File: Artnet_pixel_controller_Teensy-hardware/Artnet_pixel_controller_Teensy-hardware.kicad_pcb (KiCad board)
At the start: 2 copper layers, 122 x 57 mm, 37 parts, among them J1 Barrel_Jack_Switch, J10 Conn_01x02_Pin, J2 HR871181A, J3 Conn_01x02_Pin, J4 Conn_01x02_Pin, J5 Conn_01x02_Pin, J6 Conn_01x02_Pin, J7 Conn_01x02_Pin, J8 Conn_01x02_Pin, J9 Conn_01x02_Pin, Q1 AO3401A, SW1 SW_DIP_x08, U1 R-785.0-1.0, U3 74HC245

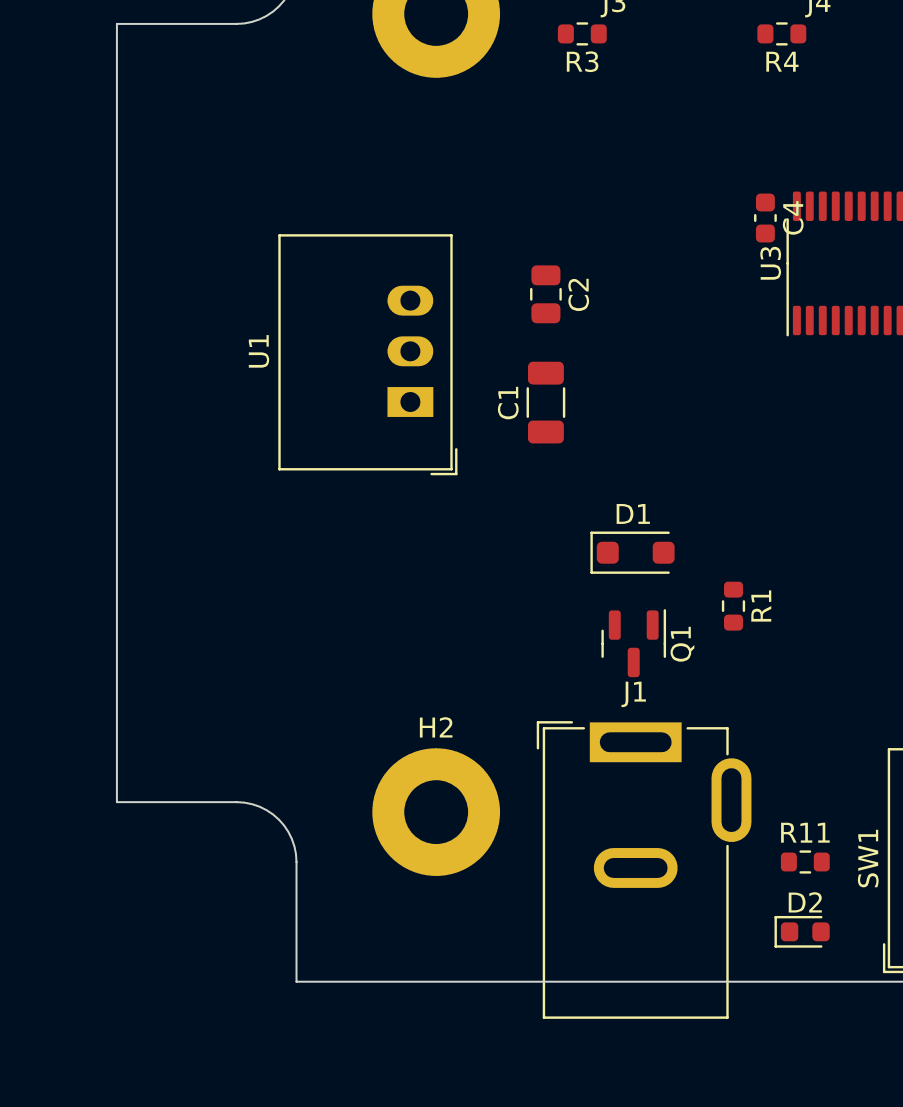
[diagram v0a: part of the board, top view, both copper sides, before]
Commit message: WS2812Serial用のピン配置に変更
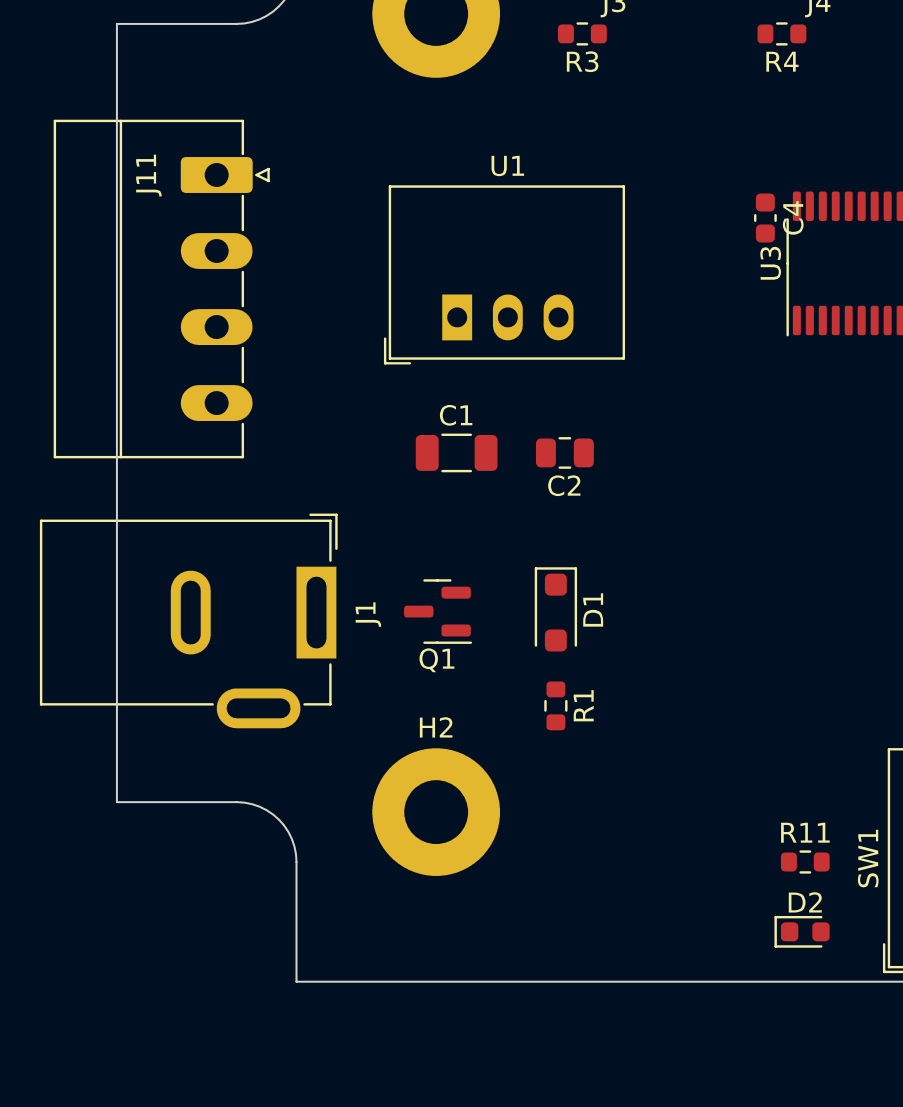
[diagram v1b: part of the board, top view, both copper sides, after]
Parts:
- added J11: Conn_01x04_Pin, Connector_Phoenix_MC:PhoenixContact_MC_1,5_4-G-3.81_1x04_P3.81mm_Horizontal, F.Cu at (95.0, 99.6)
- moved J1 17.3 mm to (100.0, 121.5), turned to -90 degrees
- moved R1 10.2 mm to (112.0, 126.2)
- moved Q1 9.97 mm to (106.1, 121.5), turned to 180 degrees
- moved C2 8.01 mm to (112.5, 113.5), turned to 180 degrees
- moved C1 5.14 mm to (107.0, 113.5), turned to 0 degrees
- moved D1 5.00 mm to (112.0, 121.5), turned to -90 degrees
- moved U1 4.85 mm to (107.1, 106.7), turned to 0 degrees
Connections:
- SW1 pad 14: Net-(U2-35) -> Net-(U2-41)
- U2 pad 10: /LED_4 -> /LED_2
- U2 pad 16: unconnected-(U2-24-Pad16) -> /LED_6
- U2 pad 21: unconnected-(U2-29-Pad21) -> /LED_7
- U2 pad 27: Net-(U2-35) -> /LED_8
- U2 pad 3: unconnected-(U2-1-Pad3) -> /LED_1
- U2 pad 33: unconnected-(U2-41-Pad33) -> Net-(U2-41)
- U2 pad 36: /LED_2 -> /LED_3
- U2 pad 39: unconnected-(U2-17-Pad39) -> /LED_4
- U2 pad 4: /LED_1 -> unconnected-(U2-2-Pad4)
- U2 pad 42: /LED_6 -> /LED_5
- U2 pad 43: /LED_7 -> unconnected-(U2-21-Pad43)
- U2 pad 7: /LED_8 -> unconnected-(U2-5-Pad7)
- U2 pad 8: /LED_5 -> unconnected-(U2-6-Pad8)
- U2 pad 9: /LED_3 -> unconnected-(U2-7-Pad9)

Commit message: プロト基板入稿データ
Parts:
- added G***: LOGO, Local_Library:ponoor_full_21x6, F.Cu at (197.0, 115.0)
- moved U1 22.0 mm to (120.0, 124.5), turned to 180 degrees
- moved D1 15.5 mm to (108.0, 106.5)
- moved Q1 15.5 mm to (102.1, 106.5)
- moved R1 15.5 mm to (108.0, 111.2)
- moved C1 13.7 mm to (120.0, 117.7), turned to 180 degrees
- moved C2 4.73 mm to (114.6, 117.7), turned to 0 degrees
- turned R10 to 0 degrees
- turned R5 to 0 degrees
- turned R6 to 0 degrees
- turned R7 to 0 degrees
- turned R8 to 0 degrees
- turned R9 to 0 degrees
- renumbered H6 to locked
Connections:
- U2 pad 15: +3.3V -> unconnected-(U2-3.3V-Pad15)
- U2 pad 46: +3.3V -> unconnected-(U2-3.3V-Pad46)
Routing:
- net GND: track 0.00 -> 536.2 mm, vias 0 -> 108
- net +5V: track 0.00 -> 127.4 mm, vias 0 -> 3
- net /LED_1: track 0.00 -> 69.6 mm
- net Net-(U3-B7): track 0.00 -> 59.1 mm
- net /LED_5: track 0.00 -> 52.3 mm
- net /LED_2: track 0.00 -> 50.6 mm
- net Net-(U3-B6): track 0.00 -> 49.3 mm
- net /LED_4: track 0.00 -> 45.4 mm
- net Net-(U3-B5): track 0.00 -> 40.0 mm
- net /LED_3: track 0.00 -> 38.5 mm
- net Net-(U2-LED): track 0.00 -> 37.6 mm, vias 0 -> 1
- net Net-(D1-K): track 0.00 -> 33.5 mm
- net /LED_6: track 0.00 -> 32.4 mm
- net Net-(U2-41): track 0.00 -> 30.7 mm
- net Net-(U3-B4): track 0.00 -> 30.5 mm
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- added copper zone on B.Cu, net GND
- added copper zone on F.Cu, net GND
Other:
- outline, holes or cut-outs redrawn
- board text added: "+"
- board text added: "-"
- board text added: "1"
- board text added: "128"
- board text added: "16"
- board text added: "2"
- board text added: "2023-04-06"
- board text added: "3"
- board text added: "32"
- board text added: "4"
- board text added: "5"
- board text added: "6"
- board text added: "64"
- board text added: "7"
- board text added: "8"
- board text added: "9-24V"
- board text added: "Artnet Pixel Controller rev.0.0.1 info@ponoor.com"
- board text added: "G"
- board text added: "GND"
- board text added: "ID"
- board text added: "OUT"
- board text added: "OUT1"
- board text added: "OUT2"
- board text added: "OUT3"
- board text added: "OUT4"
- board text added: "OUT5"
- board text added: "OUT6"
- board text added: "OUT7"
- board text added: "OUT8"
- board text added: "Vin: 9-24V"

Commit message: gerber data v1.0.0
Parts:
- R1: value 100k -> 10k
- R11: value 1k -> 10k
- R2: value 150 -> 220
- moved R11 30.5 mm to (153.0, 123.0), turned to -90 degrees
- moved D2 28.8 mm to (153.2, 137.8), turned to 180 degrees
- moved J11 4.74 mm to (94.7, 94.8)
- moved C3 0.75 mm to (167.2, 120.8)
- moved J2 0.64 mm to (169.6, 132.8)
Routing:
- net GND: track 536.2 -> 555.8 mm
- net Net-(D2-A): track 3.52 -> 15.2 mm
- net +5V: track 127.4 -> 117.0 mm, vias 3 -> 4
- net Net-(J11-Pin_3): track 22.8 -> 29.6 mm
- net Net-(U2-LED): track 37.6 -> 36.4 mm
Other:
- board text added: "2023-04-13"
- board text added: "Artnet Pixel Controller rev.1.0.0 info@ponoor.com"
- board text added: "J12"
- board text added: "J13"
- board text added: "J14"
- board text added: "Power"
- board text removed: "2023-04-06"
- board text removed: "Artnet Pixel Controller rev.0.0.1 info@ponoor.com"

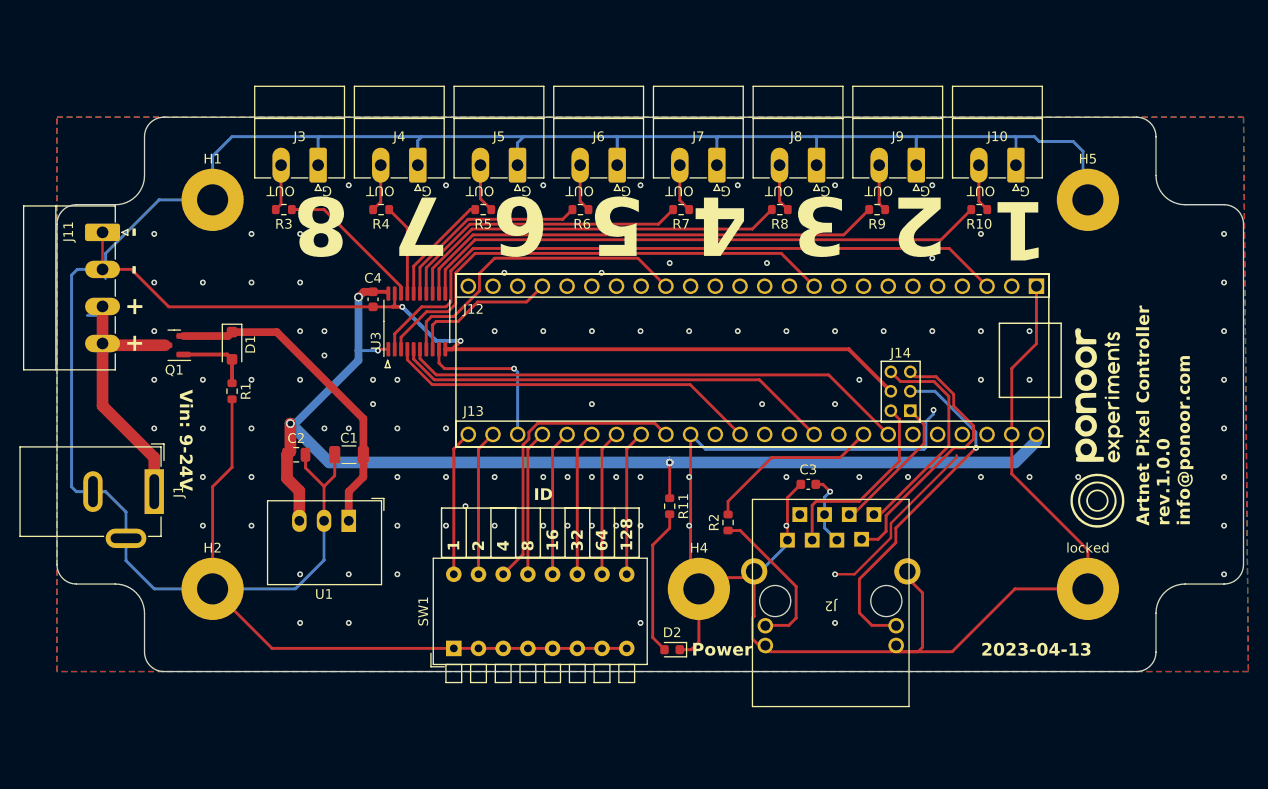
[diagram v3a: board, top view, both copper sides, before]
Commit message: LED出力の番号を入れ替え
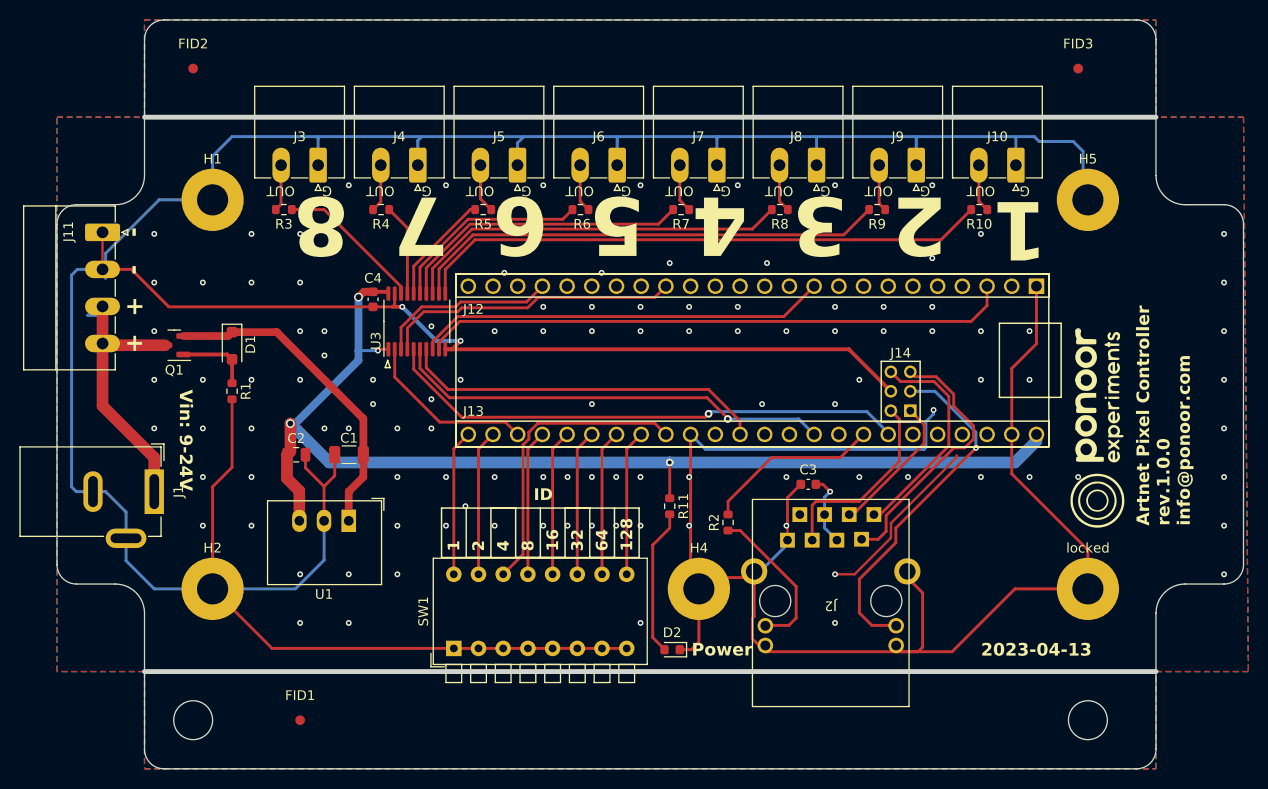
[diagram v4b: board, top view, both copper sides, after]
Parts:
- added FID1: Fiducial, Fiducial:Fiducial_1mm_Mask3mm, F.Cu at (115.0, 145.0)
- added FID2: Fiducial, Fiducial:Fiducial_1mm_Mask3mm, F.Cu at (104.0, 78.0)
- added FID3: Fiducial, Fiducial:Fiducial_1mm_Mask3mm, F.Cu at (195.0, 78.0)
- added H3: MountingHole, MountingHole:MountingHole_4mm, F.Cu at (104.0, 145.0)
- added H7: MountingHole, MountingHole:MountingHole_4mm, F.Cu at (196.0, 145.0)
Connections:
- U3 pad 2: /LED_1 -> /LED_8
- U3 pad 3: /LED_2 -> /LED_7
- U3 pad 4: /LED_3 -> /LED_6
- U3 pad 5: /LED_4 -> /LED_5
- U3 pad 6: /LED_5 -> /LED_4
- U3 pad 7: /LED_6 -> /LED_3
- U3 pad 8: /LED_7 -> /LED_2
- U3 pad 9: /LED_8 -> /LED_1
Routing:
- net /LED_1: track 69.6 -> 60.6 mm
- net /LED_2: track 50.6 -> 42.4 mm
- net /LED_7: track 15.4 -> 18.5 mm
- net /LED_6: track 32.4 -> 30.5 mm
- net /LED_5: track 52.3 -> 54.2 mm, vias 0 -> 1
- net /LED_8: track 16.3 -> 17.9 mm, vias 1 -> 0
- net /LED_3: track 38.5 -> 37.8 mm
- net /LED_4: vias 0 -> 1
- net GND: vias 108 -> 118
- added copper zone on B.Cu, net (none)
- added copper zone on F.Cu, net (none)
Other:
- board size 122 x 57 mm -> 122 x 77 mm

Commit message: PCB fabrication data
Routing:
- net +5V: track 117.0 -> 117.1 mm, vias 4 -> 5
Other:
- board text added: "2023-04-18"
- board text removed: "2023-04-13"
